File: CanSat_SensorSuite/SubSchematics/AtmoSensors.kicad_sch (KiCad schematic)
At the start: 6 parts, among them IC701 MiCS-VZ-89TE, U101 SPS30, U102 ZMOD4410AI1R

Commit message: Major sensor suite board changes, start of PCB layout
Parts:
- removed IC701: MiCS-VZ-89TE, symbol Custom_Symbol_Lib:MiCS-VZ-89TE
- added J104: Molex_01x02, 0_Connectors:502352_0201, symbol 0_Connectors:502352-0201
- added U103: STC31-C-R3, 0_Sensors:STC31-C-R3, symbol Custom_Symbol_Lib:STC31-C-R3
- C101, C102: footprint Sense&ControlBoard_footprint_library:C_0402_1005Metric -> 0_Capacitors:C_0603_1608_DensityHigh
- C103: renamed from C702; footprint Sense&ControlBoard_footprint_library:C_0402_1005Metric -> 0_Capacitors:C_0603_1608_DensityHigh
- J101: renamed from U101; footprint (none) -> 0_Connectors:JST-S5B-ZR
- U102: footprint ZMOD4410AI1R -> 0_Sensors:ZMOD4410AI1R
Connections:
- net +3V3: now also U103.6 (VCC)
- net GND: now also J104.MP1, J104.MP2, U103.1 (GND), U103.11 (GND), U103.13 (GND), U103.3 (ADDR), U103.5 (GND), U103.9 (GND)
- net I2C_SCL: now also J104.2, U103.4 (SCL)
- net I2C_SDA: now also J104.1, U103.7 (SDA)
- new net: U103.10 (NC), U103.12 (NC), U103.2 (NC), U103.8 (NC)
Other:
- note added: "7-Channel Photodiode Array"
- note added: "CO2 Concentration in Air"
- note added: "Connector MPN - JST S5B-ZR - THT Side Entry"
- note added: "Gas Sensor Module, CO2"
- note added: "I2C Address - 0x29"
- note added: "IR (1000nm) to UVC (230nm)"
- note added: "SRAD Photonics Payload"
- note added: "STC31-C-R3"
- moved on the sheet: C101, C102, C103, J101, U102

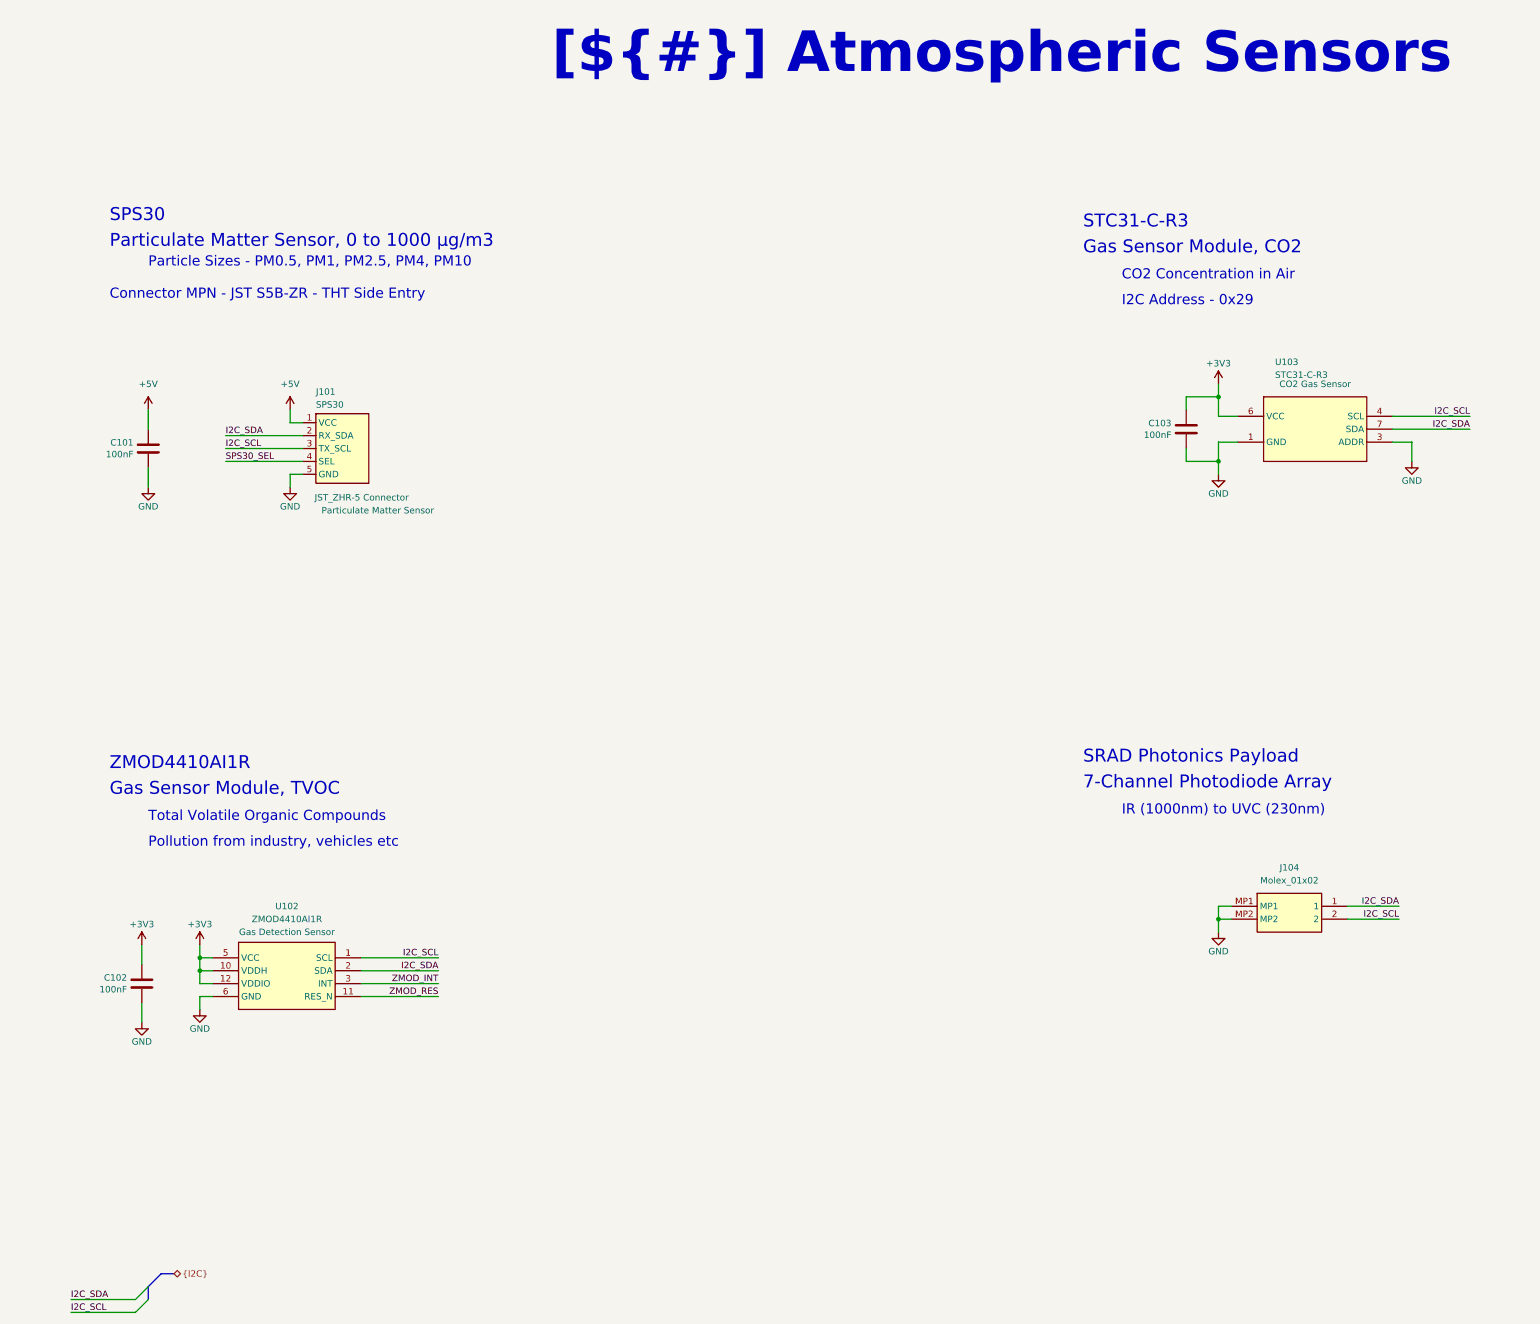
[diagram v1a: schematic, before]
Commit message: Minor schematic adjustments
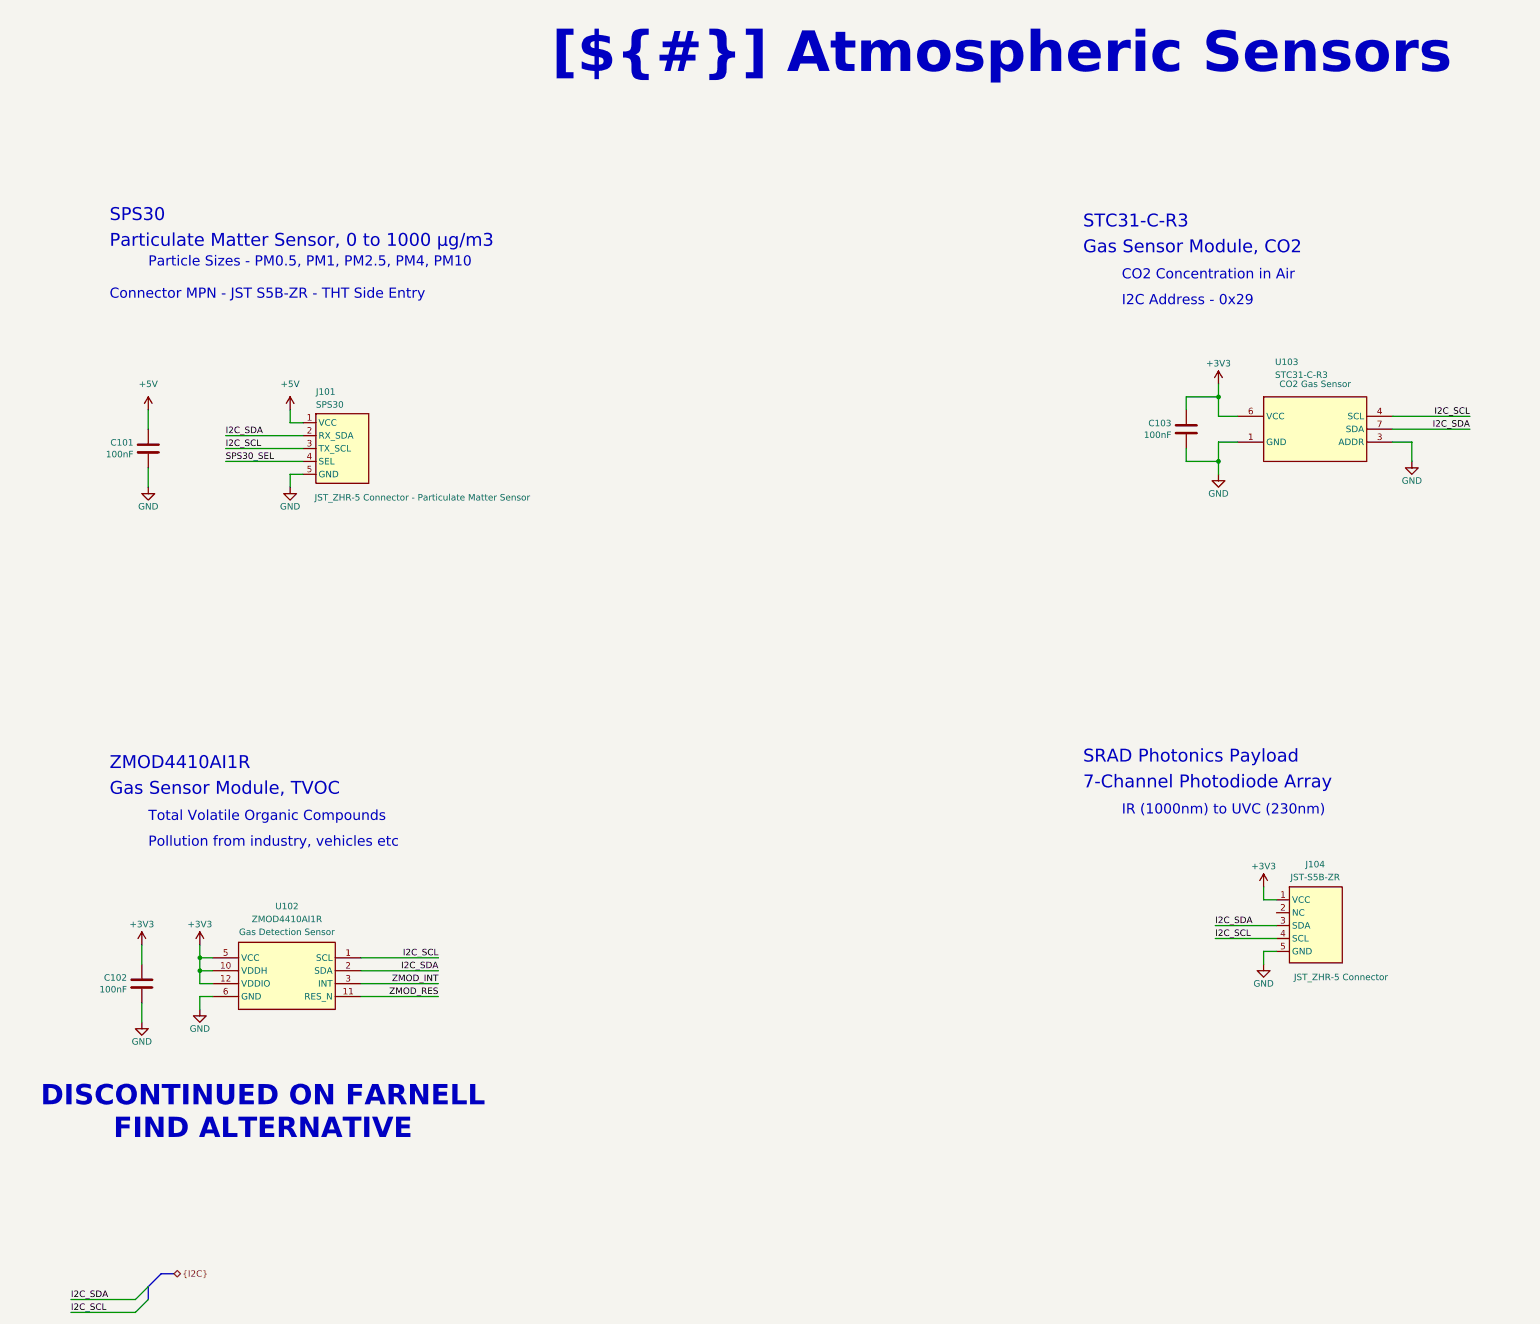
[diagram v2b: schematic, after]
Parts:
- removed J104: Molex_01x02, 0_Connectors:502352_0201, symbol 0_Connectors:502352-0201
- added J104: JST-S5B-ZR, 0_Connectors:JST-S5B-ZR, symbol Custom_Symbol_Lib:JST-S5B-ZR
- C101, C102, C103: MPN (none) -> GPC0402104; Package (none) -> C0603; Supplier (none) -> Generic
- J101: Description2 Particulate Matter Sensor -> (none); Supplier (none) -> Farnell
- U102: Height 0.77 -> (none); MPN (none) -> ZMOD4410AI1R; Manufacturer_Name Renesas Electronics -> (none); Manufacturer_Part_Number ZMOD4410AI1R -> (none); Supplier (none) -> Farnell
- U103: Farnell Part Number 4468672 -> (none); Farnell Price/Stock 32.09 -> (none); Height 1.1 -> (none); MPN (none) -> STC31-C-R3; Manufacturer_Name Sensirion -> (none); Manufacturer_Part_Number STC31-C-R3 -> (none); Order Code (none) -> 4468672; Supplier (none) -> Farnell
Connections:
- net +3V3: now also J104.1 (VCC)
- net GND: now also J104.5 (GND)
- net I2C_SCL: now also J104.4 (SCL)
- net I2C_SDA: now also J104.3 (SDA)
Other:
- note added: "DISCONTINUED ON FARNELL FIND ALTERNATIVE"
